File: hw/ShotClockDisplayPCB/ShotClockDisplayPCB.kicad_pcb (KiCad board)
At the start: 2 copper layers, 55 x 55 mm, 65 parts, among them J1 PH-00041, J2 Conn_01x05_Socket, J3 Conn_01x05_Socket, J4 Conn_01x05_Socket, J5 Conn_01x05_Socket, Q1 Q_NPN_BCE, Q10 Q_NPN_BCE, Q11 Q_NPN_BCE, Q12 Q_PMOS_SGD, Q13 Q_NPN_BCE, Q14 Q_NPN_BCE, Q15 Q_NPN_BCE, Q16 Q_NPN_BCE, Q17 Q_NPN_BCE, Q18 Q_NPN_BCE, Q19 Q_NPN_BCE, Q2 Q_NPN_BCE, Q20 Q_NPN_BCE, Q3 Q_NPN_BCE, Q4 Q_NPN_BCE, Q5 Q_PMOS_SGD, Q6 Q_NPN_BCE, Q7 Q_NPN_BCE, Q8 Q_NPN_BCE, Q9 Q_NPN_BCE

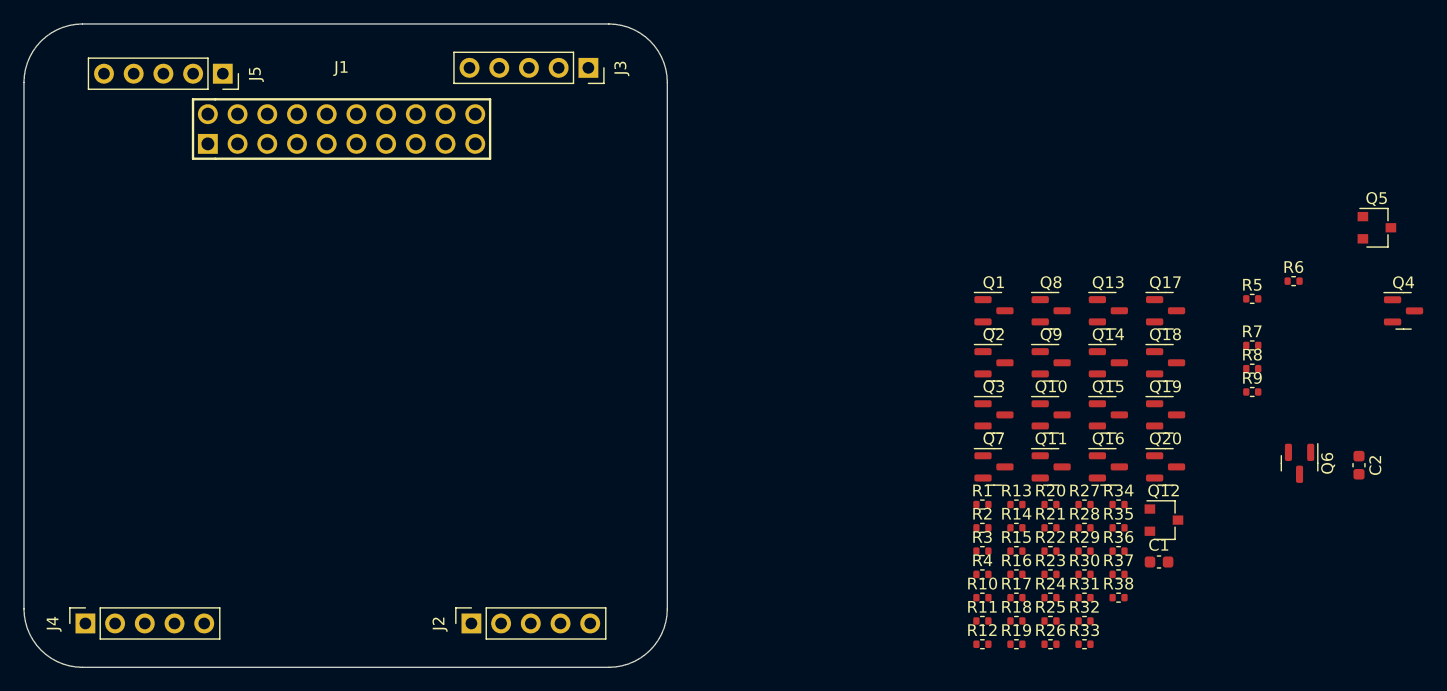
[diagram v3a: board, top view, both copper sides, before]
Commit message: Display print
Changed mainboard connector to FPC connector
Created routing for board
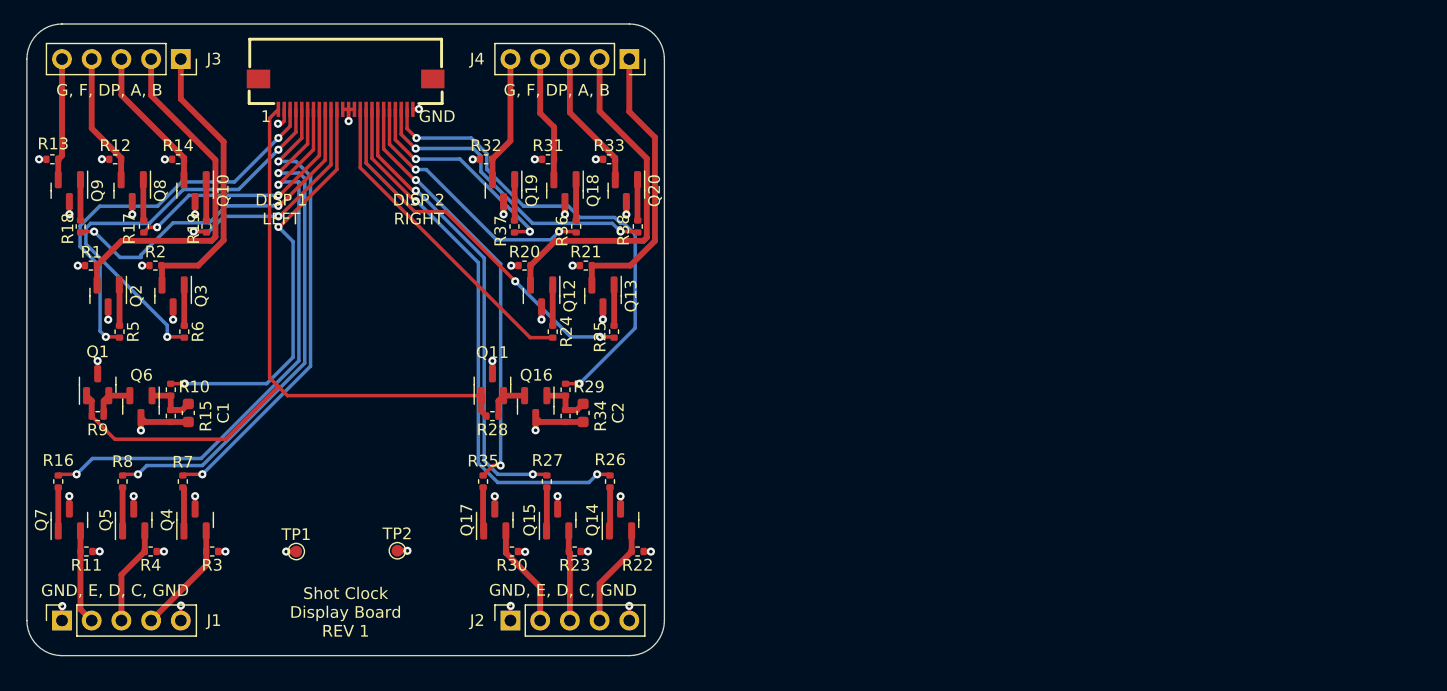
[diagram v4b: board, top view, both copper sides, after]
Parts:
- removed the J1 at (52.1, 34.0)
- added FPC1: AFC01-S24FCA-00, AFC01-S24FCA-00:FPC-SMD_P0.50-24P_FGS-XJ-H2.0, F.Cu at (52.5, 31.0)
- added TP1: TestPoint, TestPoint:TestPoint_Pad_D1.0mm, F.Cu at (48.3, 70.1)
- added TP2: TestPoint, TestPoint:TestPoint_Pad_D1.0mm, F.Cu at (56.9, 70.0)
- Q1: renamed from Q5; footprint Package_TO_SOT_SMD:SC-59 -> Package_TO_SOT_SMD:SOT-23
- Q11: renamed from Q12; footprint Package_TO_SOT_SMD:SC-59 -> Package_TO_SOT_SMD:SOT-23
- moved Q2 110.7 mm to (32.2, 48.2), turned to -90 degrees
- moved Q1 110.2 mm to (31.3, 55.8), turned to 90 degrees
- moved R1 102.8 mm to (30.7, 45.7)
- moved C1 100.2 mm to (39.0, 58.2)
- moved Q6 99.2 mm to (35.0, 57.7)
- moved R9 98.9 mm to (31.3, 58.5), turned to 180 degrees
- moved R5 96.9 mm to (33.2, 51.3), turned to -90 degrees
- moved R15 92.5 mm to (37.5, 58.5), turned to 90 degrees
- moved R10 92.5 mm to (37.5, 56.3), turned to 90 degrees
- moved R13 90.5 mm to (27.4, 36.6)
- moved R18 85.3 mm to (29.8, 42.3), turned to -90 degrees
- moved Q9 85.2 mm to (28.9, 39.2), turned to -90 degrees
- moved R12 84.0 mm to (32.8, 36.6)
- moved R14 82.8 mm to (38.2, 36.6)
- moved R16 80.2 mm to (27.9, 64.1), turned to 90 degrees
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- renumbered C2 to C1, C1 to C2, J2 to J1, J4 to J2, J5 to J4, Q13 to Q12, Q15 to Q13, Q17 to Q14, Q19 to Q15, Q11 to Q16, Q14 to Q17, Q16 to Q18, Q18 to Q19, Q4 to Q2, Q1 to Q3, Q2 to Q4, Q3 to Q5, R6 to R1, R9 to R10, R13 to R11, R15 to R12, R17 to R13, R19 to R14, R8 to R15, R12 to R16, R14 to R17, R16 to R18, R18 to R19, R25 to R20, R29 to R21, R33 to R22, R37 to R23, R23 to R24, R27 to R25, R31 to R26, R35 to R27, R22 to R28, R20 to R29, R4 to R3, R26 to R30, R30 to R31, R34 to R32, R38 to R33, R21 to R34, R24 to R35, R28 to R36, R32 to R37, R36 to R38, R11 to R4, R1 to R6, R3 to R7, R10 to R8, R7 to R9
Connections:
- J1 pad 2: /LED Driving Transistors/OUT_DISP2_SEG_E -> /LED Driving Transistors/OUT_DISP1_SEG_E
- J2 pad 2: /LED Driving Transistors/OUT_DISP1_SEG_E -> /LED Driving Transistors/OUT_DISP2_SEG_E
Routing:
- net +5V: track 0.00 -> 64.5 mm
- net /LED Driving Transistors/IN_DISP1_SEG_E: track 0.00 -> 49.5 mm, vias 0 -> 2
- net /LED Driving Transistors/IN_DISP2_SEG_C: track 0.00 -> 46.4 mm, vias 0 -> 2
- net /LED Driving Transistors/IN_DISP1_SEG_D: track 0.00 -> 44.3 mm, vias 0 -> 2
- net /LED Driving Transistors/TIM2_CH2_PWM2_SEG: track 0.00 -> 41.6 mm, vias 0 -> 2
- net /LED Driving Transistors/IN_DISP2_SEG_D: track 0.00 -> 39.9 mm, vias 0 -> 2
- net /LED Driving Transistors/IN_DISP1_SEG_C: track 0.00 -> 39.6 mm, vias 0 -> 2
- net GND: track 0.00 -> 37.6 mm, vias 0 -> 25
- net /LED Driving Transistors/IN_DISP1_SEG_B: track 0.00 -> 37.0 mm, vias 0 -> 2
- net /LED Driving Transistors/IN_DISP2_SEG_E: track 0.00 -> 36.6 mm, vias 0 -> 2
- net /LED Driving Transistors/TIM2_CH1_PWM1_SEG: track 0.00 -> 35.2 mm, vias 0 -> 2
- net /LED Driving Transistors/IN_DISP1_SEG_A: track 0.00 -> 34.5 mm, vias 0 -> 2
- net /LED Driving Transistors/IN_DISP2_SEG_B: track 0.00 -> 32.0 mm, vias 0 -> 2
- net /LED Driving Transistors/OUT_DISP1_SEG_A: track 0.00 -> 30.3 mm
- net /LED Driving Transistors/IN_DISP1_SEG_G: track 0.00 -> 29.8 mm, vias 0 -> 2
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- added copper zone on In2.Cu, net /LED Driving Transistors/PWM1_5V
- added copper zone on In2.Cu, net /LED Driving Transistors/PWM2_5V
- added copper zone on In1.Cu, net GND
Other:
- board size 55 x 55 mm -> 54.5 x 54 mm
- copper layers 2 -> 4
- board text added: "1"
- board text added: "DISP 1 LEFT"
- board text added: "DISP 2 RIGHT"
- board text added: "G, F, DP, A, B"
- board text added: "GND"
- board text added: "GND, E, D, C, GND"
- board text added: "Shot Clock Display Board REV 1"
- board text added: "x28.25 y28"
- board text added: "x28.25 y76"
- board text added: "x76.75 y28"
- board text added: "x76.75 y76"

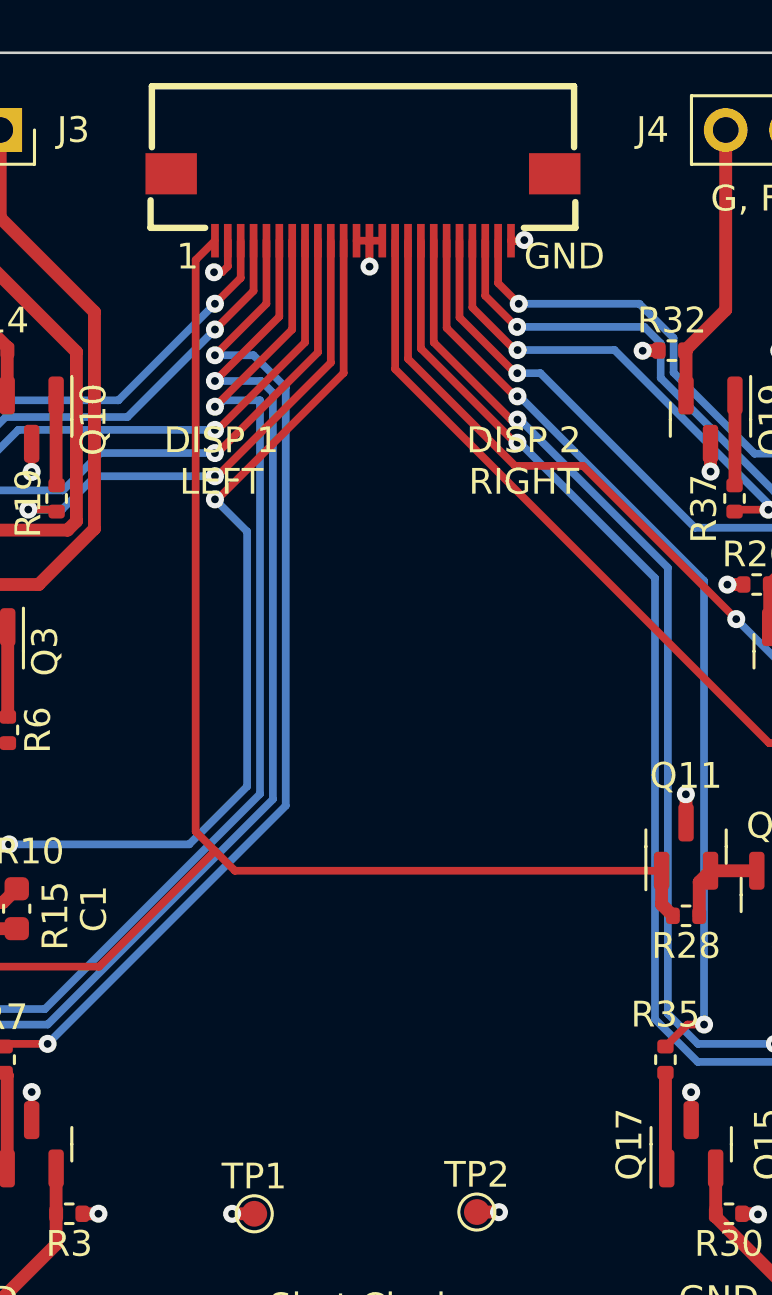
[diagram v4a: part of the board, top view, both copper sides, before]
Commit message: Added silkscreen and mounting holes
Plus JLC assembly holes
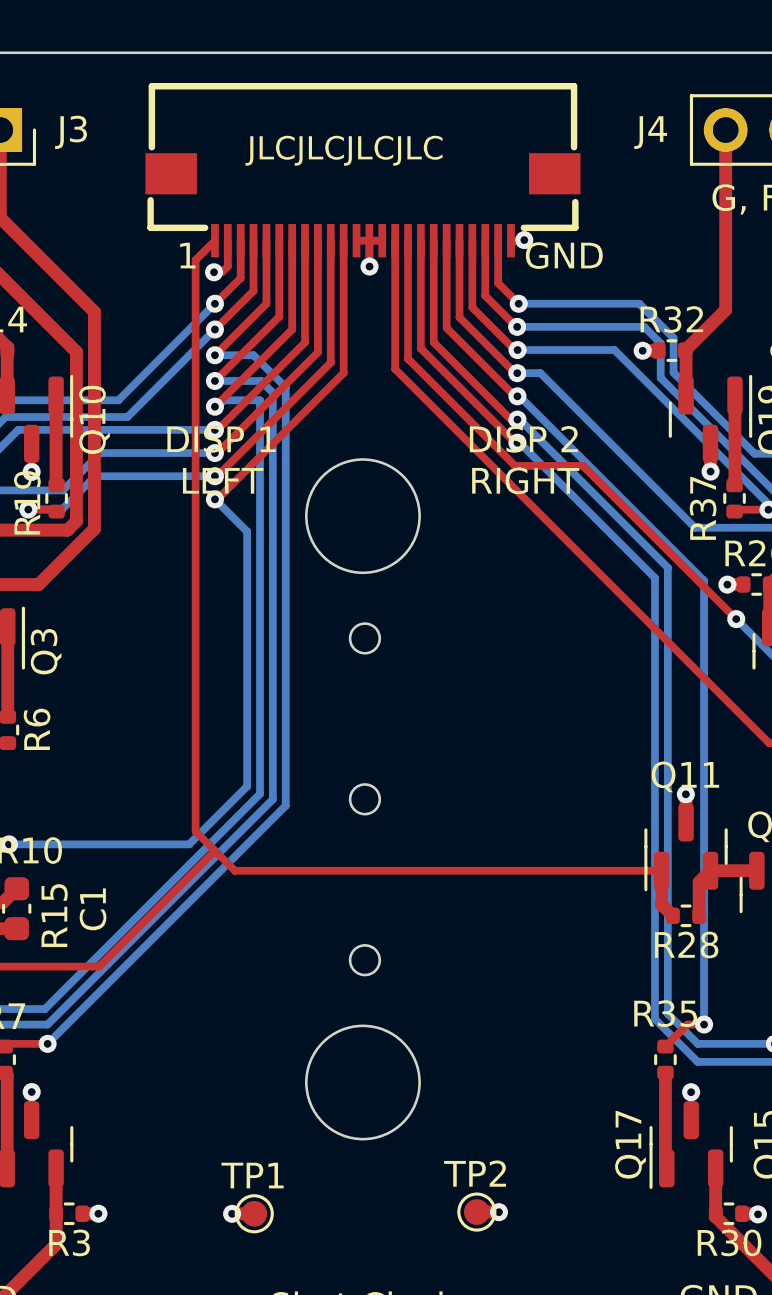
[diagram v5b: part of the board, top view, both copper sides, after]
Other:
- outline, holes or cut-outs redrawn
- board text added: "JLCJLCJLCJLC"
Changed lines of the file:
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@@
     )
   )
+  (gr_circle (center 52.5 65) (end 54.7 65)
+    (stroke (width 0.1) (type default)) (fill none) (layer "Edge.Cuts"))
+  (gr_circle (center 52.576 47.75) (end 53.152 47.75)
+    (stroke (width 0.1) (type default)) (fill none) (layer "Edge.Cuts"))
+  (gr_circle (center 52.5 43) (end 54.7 43)
+    (stroke (width 0.1) (type default)) (fill none) (layer "Edge.Cuts"))
   (gr_arc (start 28.25 79) (mid 26.12868 78.12132) (end 25.25 76)
     (stroke (width 0.1) (type default)) (layer "Edge.Cuts"))
   (gr_line (start 25.25 76) (end 25.25 28)
     (stroke (width 0.1) (type default)) (layer "Edge.Cuts"))
+  (gr_circle (center 52.576 54) (end 53.152 54)
+    (stroke (width 0.1) (type default)) (fill none) (layer "Edge.Cuts"))
   (gr_arc (start 79.75 76) (mid 78.87132 78.12132) (end 76.75 79)
     (stroke (width 0.1) (type default)) (layer "Edge.Cuts"))
+  (gr_circle (center 52.576 60.25) (end 53.152 60.25)
+    (stroke (width 0.1) (type default)) (fill none) (layer "Edge.Cuts"))
   (gr_line (start 79.75 28) (end 79.75 76)
     (stroke (width 0.1) (type default)) (layer "Edge.Cuts"))
@@
   (gr_text "GND, E, D, C, GND" (at 26.456394 74.021802) (layer "F.SilkS")
     (effects (font (size 1 1) (thickness 0.15)) (justify left bottom))
+  )
+  (gr_text "JLCJLCJLCJLC" (at 48 29.25) (layer "F.SilkS")
+    (effects (font (size 0.9 0.9) (thickness 0.15)) (justify left bottom))
   )
   (gr_text "G, F, DP, A, B" (at 66 31.25) (layer "F.SilkS")
@@
         (xy 20 20)
         (xy 20 82.5)
-        (xy 50.25 82.25)
-        (xy 50.25 20)
+        (xy 49.75 82)
+        (xy 49.75 19.75)
       )
     )
@@
     (polygon
       (pts
-        (xy 55 20)
-        (xy 55 82.5)
+        (xy 55.5 20)
+        (xy 55.5 82.5)
         (xy 85.25 82.25)
         (xy 85.25 20)

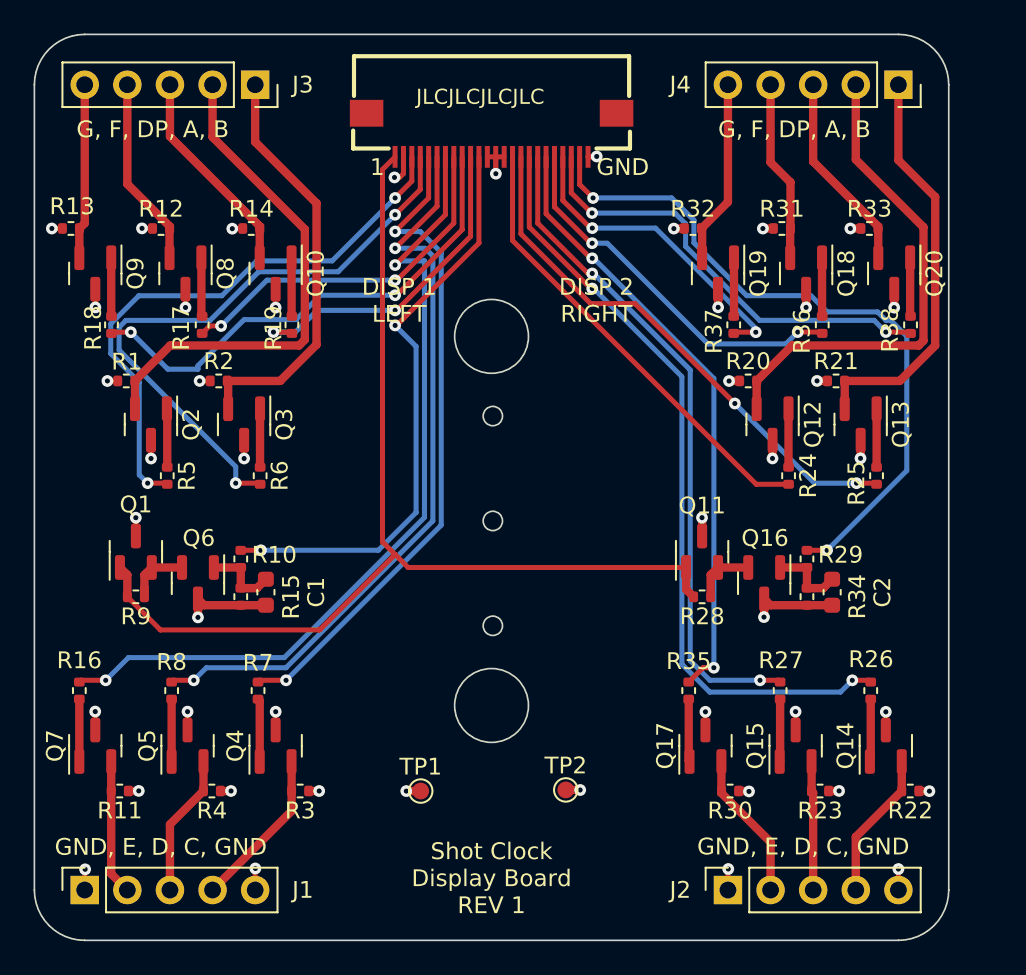
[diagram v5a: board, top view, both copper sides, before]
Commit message: Cleaned second print
and added new connectors, pinout and removed all REV1 stuff.
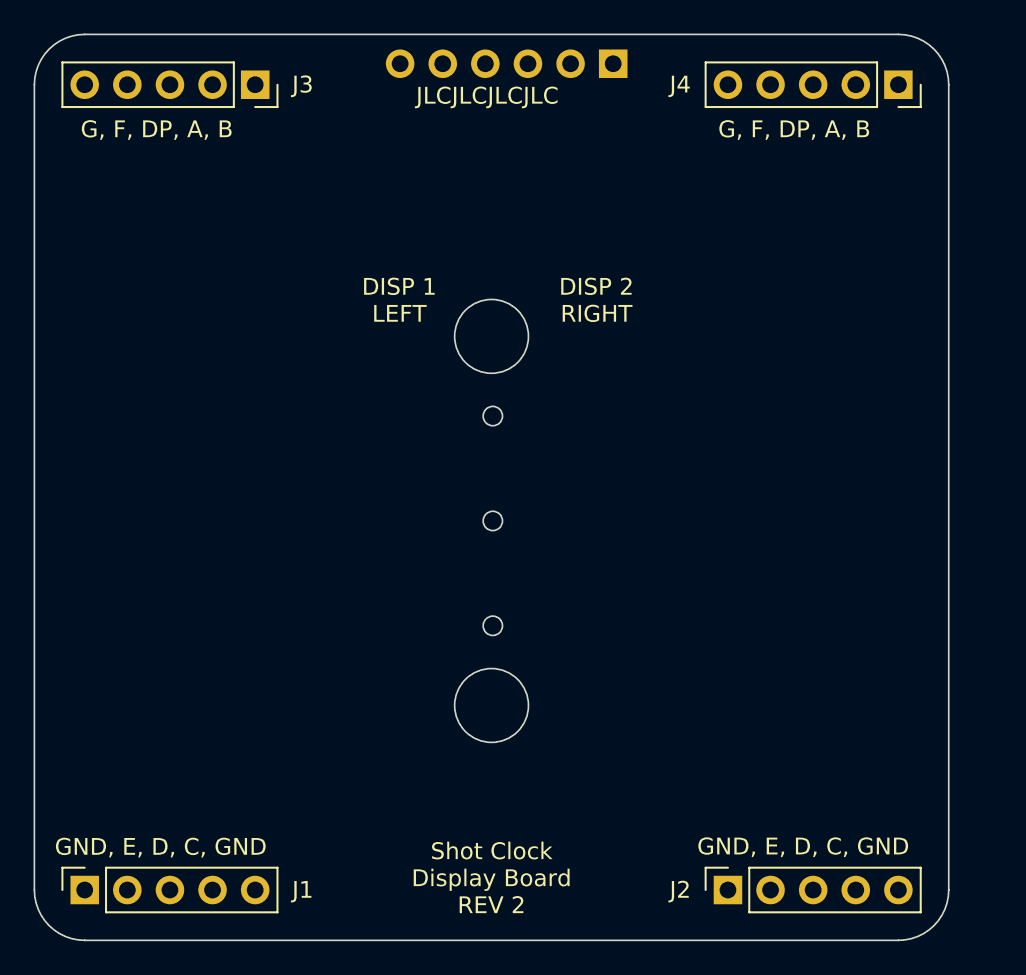
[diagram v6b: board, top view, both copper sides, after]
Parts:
- removed C1, C2: 10n, Capacitor_SMD:C_0603_1608Metric
- removed FPC1: AFC01-S24FCA-00, AFC01-S24FCA-00:FPC-SMD_P0.50-24P_FGS-XJ-H2.0
- removed Q1, Q11: Q_PMOS_SGD, Package_TO_SOT_SMD:SOT-23
- removed Q10, Q12, Q13, Q14, Q15, Q16, Q17, Q18, Q19, Q2, Q20, Q3, Q4, Q5, Q6, Q7, Q8, Q9: Q_NPN_BCE, Package_TO_SOT_SMD:SOT-23
- removed R1, R11, R12, R13, R14, R2, R20, R21, R22, R23, R3, R30, R31, R32, R33, R4: 100R, Resistor_SMD:R_0402_1005Metric
- removed R10, R29: 1k, Resistor_SMD:R_0402_1005Metric
- removed R15, R16, R17, R18, R19, R24, R25, R26, R27, R34, R35, R36, R37, R38, R5, R6, R7, R8: 10k, Resistor_SMD:R_0402_1005Metric
- removed R28, R9: 100k, Resistor_SMD:R_0402_1005Metric
- removed TP1, TP2: TestPoint, TestPoint:TestPoint_Pad_D1.0mm
- added J5: Conn_01x06_Pin, Connector_PinHeader_2.54mm:PinHeader_1x06_P2.54mm_Vertical, B.Cu at (59.8, 26.8)
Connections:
- J1 pad 2: /LED Driving Transistors/OUT_DISP1_SEG_E -> /Segment Display Connectors/SEG1_E
- J1 pad 3: /LED Driving Transistors/OUT_DISP1_SEG_D -> /Segment Display Connectors/SEG1_D
- J1 pad 4: /LED Driving Transistors/OUT_DISP1_SEG_C -> /Segment Display Connectors/SEG1_C
- J2 pad 2: /LED Driving Transistors/OUT_DISP2_SEG_E -> /Segment Display Connectors/SEG2_E
- J2 pad 3: /LED Driving Transistors/OUT_DISP2_SEG_D -> /Segment Display Connectors/SEG2_D
- J2 pad 4: /LED Driving Transistors/OUT_DISP2_SEG_C -> /Segment Display Connectors/SEG2_C
- J3 pad 1: /LED Driving Transistors/OUT_DISP1_SEG_B -> /Segment Display Connectors/SEG1_B
- J3 pad 2: /LED Driving Transistors/OUT_DISP1_SEG_A -> /Segment Display Connectors/SEG1_A
- J3 pad 3: /LED Driving Transistors/OUT_DISP1_SEG_DP -> /Segment Display Connectors/SEG1_DP
- J3 pad 4: /LED Driving Transistors/OUT_DISP1_SEG_F -> /Segment Display Connectors/SEG1_F
- J3 pad 5: /LED Driving Transistors/OUT_DISP1_SEG_G -> /Segment Display Connectors/SEG1_G
- J4 pad 1: /LED Driving Transistors/OUT_DISP2_SEG_B -> /Segment Display Connectors/SEG2_B
- J4 pad 2: /LED Driving Transistors/OUT_DISP2_SEG_A -> /Segment Display Connectors/SEG2_A
- J4 pad 3: /LED Driving Transistors/OUT_DISP2_SEG_DP -> /Segment Display Connectors/SEG2_DP
- J4 pad 4: /LED Driving Transistors/OUT_DISP2_SEG_F -> /Segment Display Connectors/SEG2_F
- J4 pad 5: /LED Driving Transistors/OUT_DISP2_SEG_G -> /Segment Display Connectors/SEG2_G
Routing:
- net +5V: track 64.5 -> 0.00 mm
- net /LED Driving Transistors/IN_DISP1_SEG_E: track 49.5 -> 0.00 mm, vias 2 -> 0
- net /LED Driving Transistors/IN_DISP2_SEG_C: track 46.4 -> 0.00 mm, vias 2 -> 0
- net /LED Driving Transistors/IN_DISP1_SEG_D: track 44.3 -> 0.00 mm, vias 2 -> 0
- net /LED Driving Transistors/TIM2_CH2_PWM2_SEG: track 41.6 -> 0.00 mm, vias 2 -> 0
- net /LED Driving Transistors/IN_DISP2_SEG_D: track 39.9 -> 0.00 mm, vias 2 -> 0
- net /LED Driving Transistors/IN_DISP1_SEG_C: track 39.6 -> 0.00 mm, vias 2 -> 0
- net GND: track 37.6 -> 0.00 mm, vias 25 -> 0
- net /LED Driving Transistors/IN_DISP1_SEG_B: track 37.0 -> 0.00 mm, vias 2 -> 0
- net /LED Driving Transistors/IN_DISP2_SEG_E: track 36.6 -> 0.00 mm, vias 2 -> 0
- net /LED Driving Transistors/TIM2_CH1_PWM1_SEG: track 35.2 -> 0.00 mm, vias 2 -> 0
- net /LED Driving Transistors/IN_DISP1_SEG_A: track 34.5 -> 0.00 mm, vias 2 -> 0
- net /LED Driving Transistors/IN_DISP2_SEG_B: track 32.0 -> 0.00 mm, vias 2 -> 0
- net /LED Driving Transistors/OUT_DISP1_SEG_A: track 30.3 -> 0.00 mm
- net /LED Driving Transistors/IN_DISP1_SEG_G: track 29.8 -> 0.00 mm, vias 2 -> 0
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- removed copper zone on In2.Cu, net /LED Driving Transistors/PWM1_5V
- removed copper zone on In2.Cu, net /LED Driving Transistors/PWM2_5V
- removed copper zone on In1.Cu, net GND
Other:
- board text added: "Shot Clock Display Board REV 2"
- board text removed: "1"
- board text removed: "GND"
- board text removed: "Shot Clock Display Board REV 1"
